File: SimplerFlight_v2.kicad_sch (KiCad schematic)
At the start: 19 parts, among them J2 Conn_01x04_Pin, J3 Conn_01x04_Pin, J4 Conn_01x04_Pin, J5 Conn_01x04_Pin, SW1 SW_SPDT, U2 STM32F401RETx, Y1 16MHz

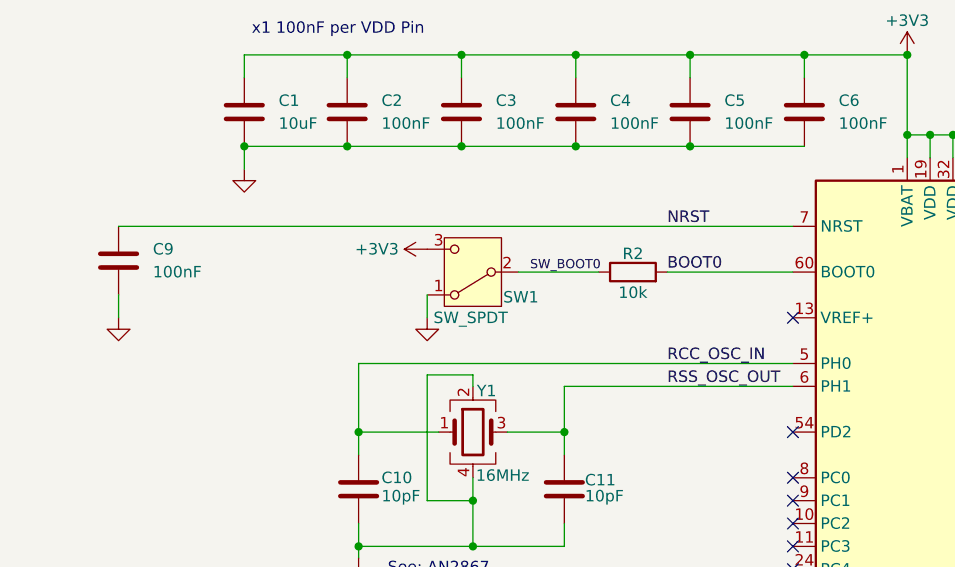
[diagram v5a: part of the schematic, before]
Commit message: Upload architecture diagram, start sensor schematic, add simulation files
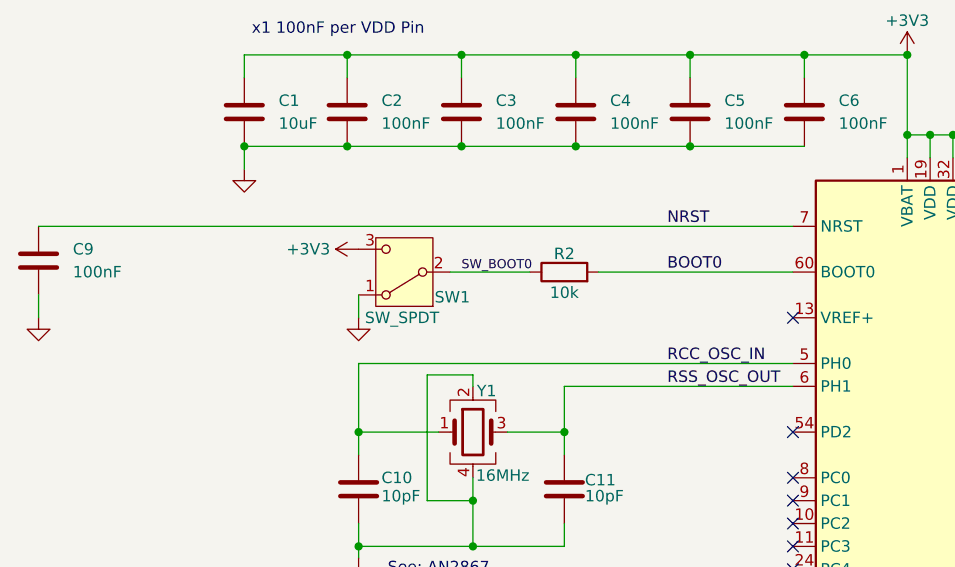
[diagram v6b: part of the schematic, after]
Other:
- moved on the sheet: C9, R2, SW1
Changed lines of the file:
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@@
 	(wire
 		(pts
-			(xy 25.4 45.72) (xy 100.33 45.72)
+			(xy 16.51 45.72) (xy 100.33 45.72)
 		)
 		(stroke
@@
 	(wire
 		(pts
-			(xy 86.36 50.8) (xy 100.33 50.8)
+			(xy 76.2 26.67) (xy 76.2 29.21)
 		)
 		(stroke
@@
 	(wire
 		(pts
-			(xy 76.2 26.67) (xy 76.2 29.21)
+			(xy 172.72 111.76) (xy 172.72 125.73)
 		)
 		(stroke
@@
 	(wire
 		(pts
-			(xy 172.72 111.76) (xy 172.72 125.73)
+			(xy 39.37 29.21) (xy 39.37 26.67)
 		)
 		(stroke
@@
 	(wire
 		(pts
-			(xy 39.37 29.21) (xy 39.37 26.67)
+			(xy 185.42 95.25) (xy 185.42 93.98)
 		)
 		(stroke
@@
 	(wire
 		(pts
-			(xy 185.42 95.25) (xy 185.42 93.98)
+			(xy 76.2 36.83) (xy 88.9 36.83)
 		)
 		(stroke
@@
 	(wire
 		(pts
-			(xy 76.2 36.83) (xy 88.9 36.83)
+			(xy 209.55 101.6) (xy 209.55 100.33)
 		)
 		(stroke
@@
 	(wire
 		(pts
-			(xy 209.55 101.6) (xy 209.55 100.33)
+			(xy 74.93 78.74) (xy 74.93 81.28)
 		)
 		(stroke
@@
 	(wire
 		(pts
-			(xy 74.93 78.74) (xy 74.93 81.28)
+			(xy 78.74 50.8) (xy 100.33 50.8)
 		)
 		(stroke
@@
 	(wire
 		(pts
-			(xy 25.4 53.34) (xy 25.4 55.88)
+			(xy 16.51 53.34) (xy 16.51 55.88)
 		)
 		(stroke
@@
 	(wire
 		(pts
-			(xy 59.69 55.88) (xy 59.69 53.34)
+			(xy 52.07 55.88) (xy 52.07 53.34)
 		)
 		(stroke
@@
 	(wire
 		(pts
-			(xy 69.85 50.8) (xy 78.74 50.8)
+			(xy 62.23 50.8) (xy 71.12 50.8)
 		)
 		(stroke
@@
 	)
 	(label "SW_BOOT0"
-		(at 71.12 50.8 0)
+		(at 63.5 50.8 0)
 		(effects
 			(font
@@
 	(symbol
 		(lib_id "Device:C")
-		(at 25.4 49.53 0)
+		(at 16.51 49.53 0)
 		(unit 1)
 		(exclude_from_sim no)
@@
 		(fields_autoplaced yes)
 		(property "Reference" "C9"
-			(at 29.21 48.2599 0)
+			(at 20.32 48.2599 0)
 			(effects
 				(font
@@
 		)
 		(property "Value" "100nF"
-			(at 29.21 50.7999 0)
+			(at 20.32 50.7999 0)
 			(effects
 				(font
@@
 		)
 		(property "Footprint" "Capacitor_SMD:C_0805_2012Metric"
-			(at 26.3652 53.34 0)
+			(at 17.4752 53.34 0)
 			(effects
 				(font
@@
 		)
 		(property "Datasheet" "~"
-			(at 25.4 49.53 0)
+			(at 16.51 49.53 0)
 			(effects
 				(font
@@
 		)
 		(property "Description" "Unpolarized capacitor"
-			(at 25.4 49.53 0)
+			(at 16.51 49.53 0)
 			(effects
 				(font
@@
 	(symbol
 		(lib_id "Device:R")
-		(at 82.55 50.8 90)
+		(at 74.93 50.8 90)
 		(unit 1)
 		(exclude_from_sim no)
@@
 		(dnp no)
 		(property "Reference" "R2"
-			(at 82.55 48.768 90)
+			(at 74.93 48.768 90)
 			(effects
 				(font
@@
 		)
 		(property "Value" "10k"
-			(at 82.55 53.086 90)
+			(at 74.93 53.086 90)
 			(effects
 				(font
@@
 		)
 		(property "Footprint" "Capacitor_SMD:C_0805_2012Metric"
-			(at 82.55 52.578 90)
+			(at 74.93 52.578 90)
 			(effects
 				(font
@@
 		)
 		(property "Datasheet" "~"
-			(at 82.55 50.8 0)
+			(at 74.93 50.8 0)
 			(effects
 				(font
@@
 		)
 		(property "Description" "Resistor"
-			(at 82.55 50.8 0)
+			(at 74.93 50.8 0)
 			(effects
 				(font
@@
 	(symbol
 		(lib_id "power:+3V3")
-		(at 59.69 48.26 90)
+		(at 52.07 48.26 90)
 		(unit 1)
 		(exclude_from_sim no)
@@
 		(dnp no)
 		(property "Reference" "#PWR06"
-			(at 63.5 48.26 0)
+			(at 55.88 48.26 0)
 			(effects
 				(font
@@
 		)
 		(property "Value" "+3V3"
-			(at 54.102 48.26 90)
+			(at 46.482 48.26 90)
 			(effects
 				(font
@@
 		)
 		(property "Footprint" ""
-			(at 59.69 48.26 0)
+			(at 52.07 48.26 0)
 			(effects
 				(font
@@
 		)
 		(property "Datasheet" ""
-			(at 59.69 48.26 0)
+			(at 52.07 48.26 0)
 			(effects
 				(font
@@
 		)
 		(property "Description" "Power symbol creates a global label with name \"+3V3\""
-			(at 59.69 48.26 0)
+			(at 52.07 48.26 0)
 			(effects
 				(font
@@
 	(symbol
 		(lib_id "Switch:SW_SPDT")
-		(at 64.77 50.8 180)
+		(at 57.15 50.8 180)
 		(unit 1)
 		(exclude_from_sim no)
@@
 		(dnp no)
 		(property "Reference" "SW1"
-			(at 70.104 53.594 0)
+			(at 62.484 53.594 0)
 			(effects
 				(font
@@
 		)
 		(property "Value" "SW_SPDT"
-			(at 64.516 55.88 0)
+			(at 56.896 55.88 0)
 			(effects
 				(font
@@
 		)
 		(property "Footprint" "Button_Switch_SMD:SW_SPDT_PCM12"
-			(at 64.77 50.8 0)
+			(at 57.15 50.8 0)
 			(effects
 				(font
@@
 		)
 		(property "Datasheet" "~"
-			(at 64.77 43.18 0)
+			(at 57.15 43.18 0)
 			(effects
 				(font
@@
 		)
 		(property "Description" "Switch, single pole double throw"
-			(at 64.77 50.8 0)
+			(at 57.15 50.8 0)
 			(effects
 				(font
@@
 	(symbol
 		(lib_id "power:GND")
-		(at 59.69 55.88 0)
+		(at 52.07 55.88 0)
 		(unit 1)
 		(exclude_from_sim no)
@@
 		(fields_autoplaced yes)
 		(property "Reference" "#PWR08"
-			(at 59.69 62.23 0)
+			(at 52.07 62.23 0)
 			(effects
 				(font
@@
 		)
 		(property "Value" "GND"
-			(at 59.69 60.96 0)
+			(at 52.07 60.96 0)
 			(effects
 				(font
@@
 		)
 		(property "Footprint" ""
-			(at 59.69 55.88 0)
+			(at 52.07 55.88 0)
 			(effects
 				(font
@@
 		)
 		(property "Datasheet" ""
-			(at 59.69 55.88 0)
+			(at 52.07 55.88 0)
 			(effects
 				(font
@@
 		)
 		(property "Description" "Power symbol creates a global label with name \"GND\" , ground"
-			(at 59.69 55.88 0)
+			(at 52.07 55.88 0)
 			(effects
 				(font
@@
 	(symbol
 		(lib_id "power:GND")
-		(at 25.4 55.88 0)
+		(at 16.51 55.88 0)
 		(unit 1)
 		(exclude_from_sim no)
@@
 		(fields_autoplaced yes)
 		(property "Reference" "#PWR07"
-			(at 25.4 62.23 0)
+			(at 16.51 62.23 0)
 			(effects
 				(font
@@
 		)
 		(property "Value" "GND"
-			(at 25.4 60.96 0)
+			(at 16.51 60.96 0)
 			(effects
 				(font
@@
 		)
 		(property "Footprint" ""
-			(at 25.4 55.88 0)
+			(at 16.51 55.88 0)
 			(effects
 				(font
@@
 		)
 		(property "Datasheet" ""
-			(at 25.4 55.88 0)
+			(at 16.51 55.88 0)
 			(effects
 				(font
@@
 		)
 		(property "Description" "Power symbol creates a global label with name \"GND\" , ground"
-			(at 25.4 55.88 0)
+			(at 16.51 55.88 0)
 			(effects
 				(font
